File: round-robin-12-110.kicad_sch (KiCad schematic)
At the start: 242 parts

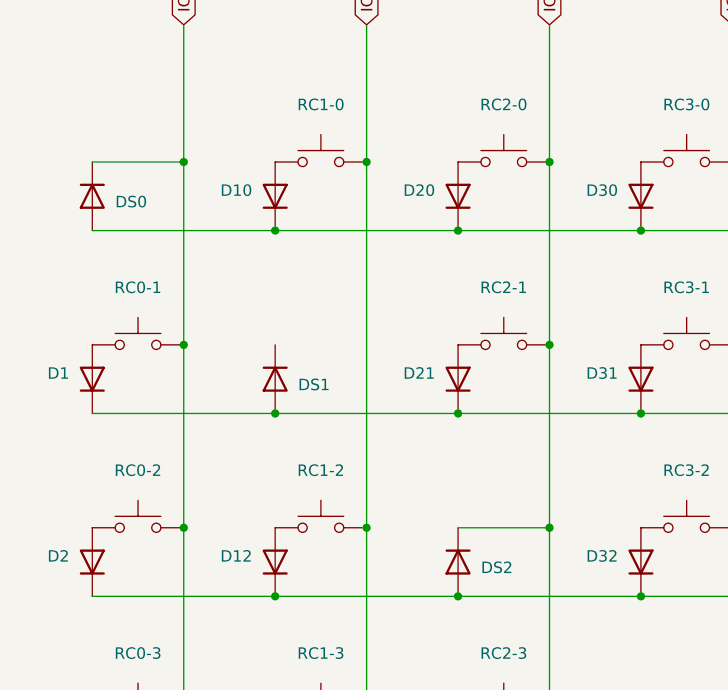
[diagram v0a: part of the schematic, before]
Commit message: Add missing connector on DS1
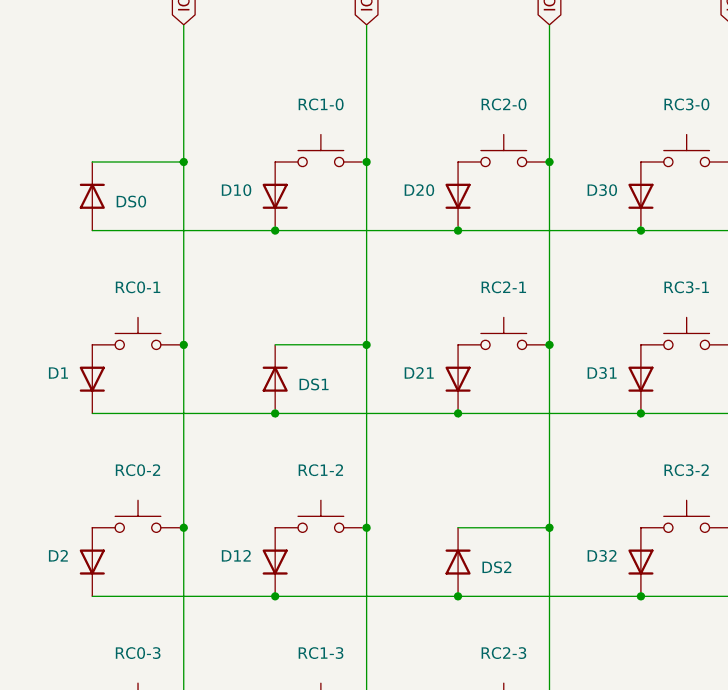
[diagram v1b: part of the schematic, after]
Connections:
- net IO 1: now also DS1.1 (K)
